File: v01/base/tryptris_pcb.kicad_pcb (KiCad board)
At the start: 2 copper layers, 298.8 x 122 mm, 141 parts, among them J1 USB_C_Receptacle_USB2.0, J2 I2C-L, J3 I2C-R, SW1 Reset, U1 ATmega32U4, U2 MCP23017, U4 HOLE, Y1 16Mhz

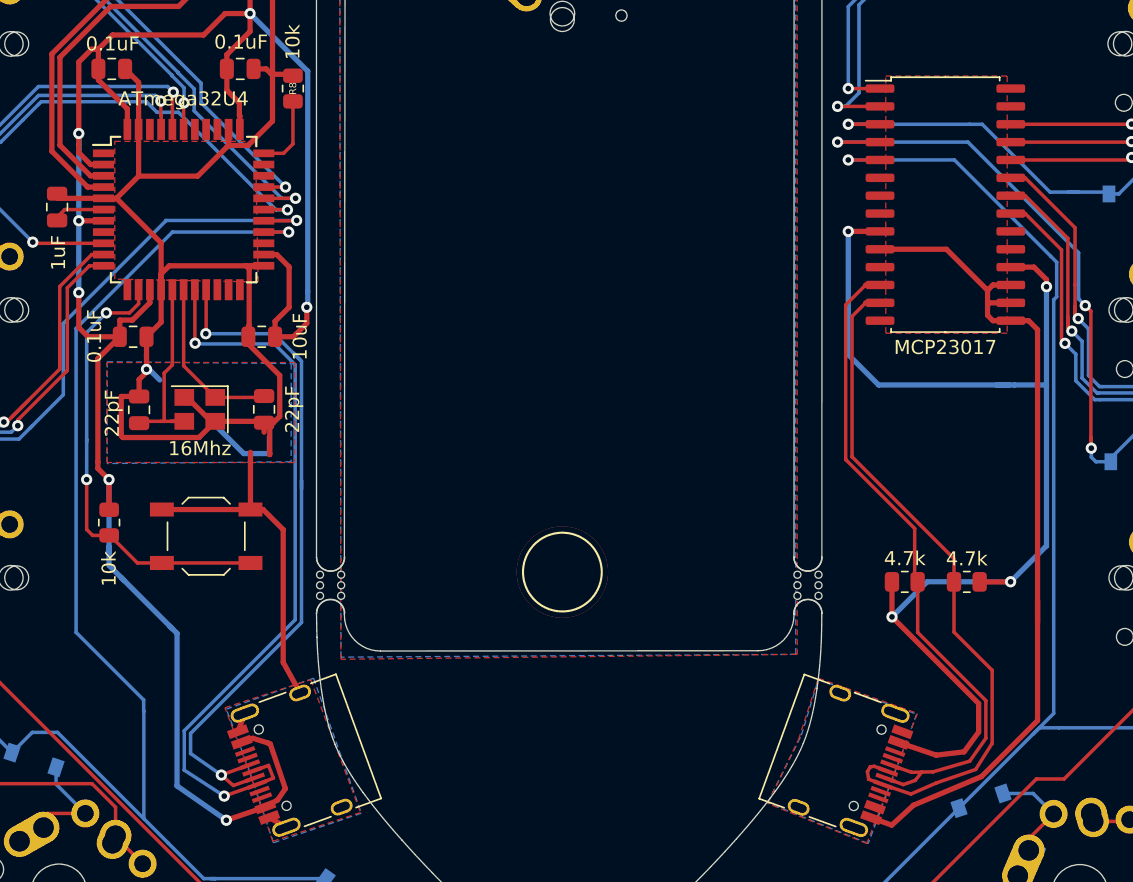
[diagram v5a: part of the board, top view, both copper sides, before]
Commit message: Move I2C resistors to MCU side
This lets the right side be simpler and visually cleaner. It also
matches the component layout of the bling version.
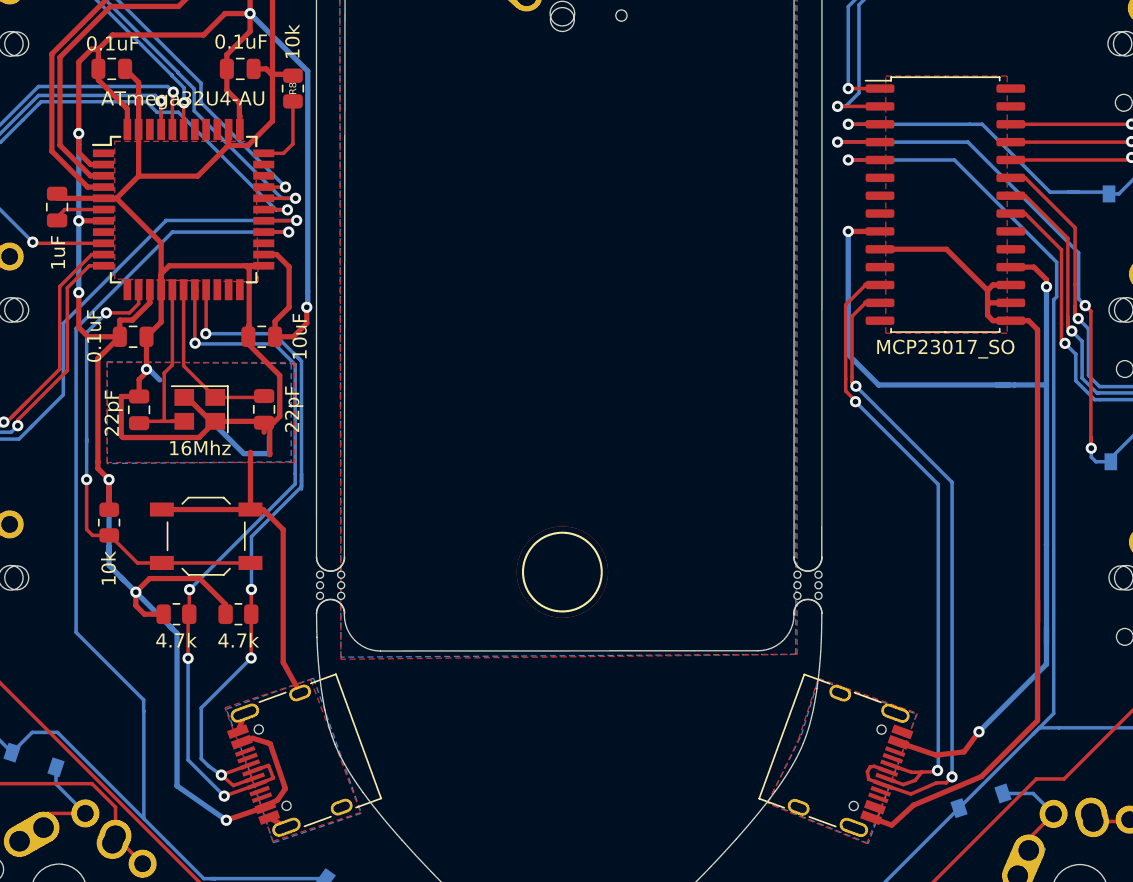
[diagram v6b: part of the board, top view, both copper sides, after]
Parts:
- U1: value ATmega32U4 -> ATmega32U4-AU
- U2: value MCP23017 -> MCP23017_SO
- moved R7 51.9 mm to (152.5, 104.7)
- moved R6 51.9 mm to (148.0, 104.7)
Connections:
- R6 pad 1: SCL-R -> SCL-L
- R6 pad 2: VBUS -> +5V
- R7 pad 1: SDA-R -> +5V
- R7 pad 2: VBUS -> SDA-L
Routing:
- net VBUS: track 84.2 -> 71.8 mm, vias 4 -> 3
- net +5V: track 156.2 -> 167.7 mm, vias 7 -> 8
- net SCL-R: track 48.4 -> 45.4 mm, vias 0 -> 2
- net SDA-R: track 49.7 -> 46.8 mm, vias 0 -> 2
- net SCL-L: track 53.4 -> 53.1 mm, vias 2 -> 4
- net SDA-L: track 50.7 -> 50.4 mm, vias 2 -> 4

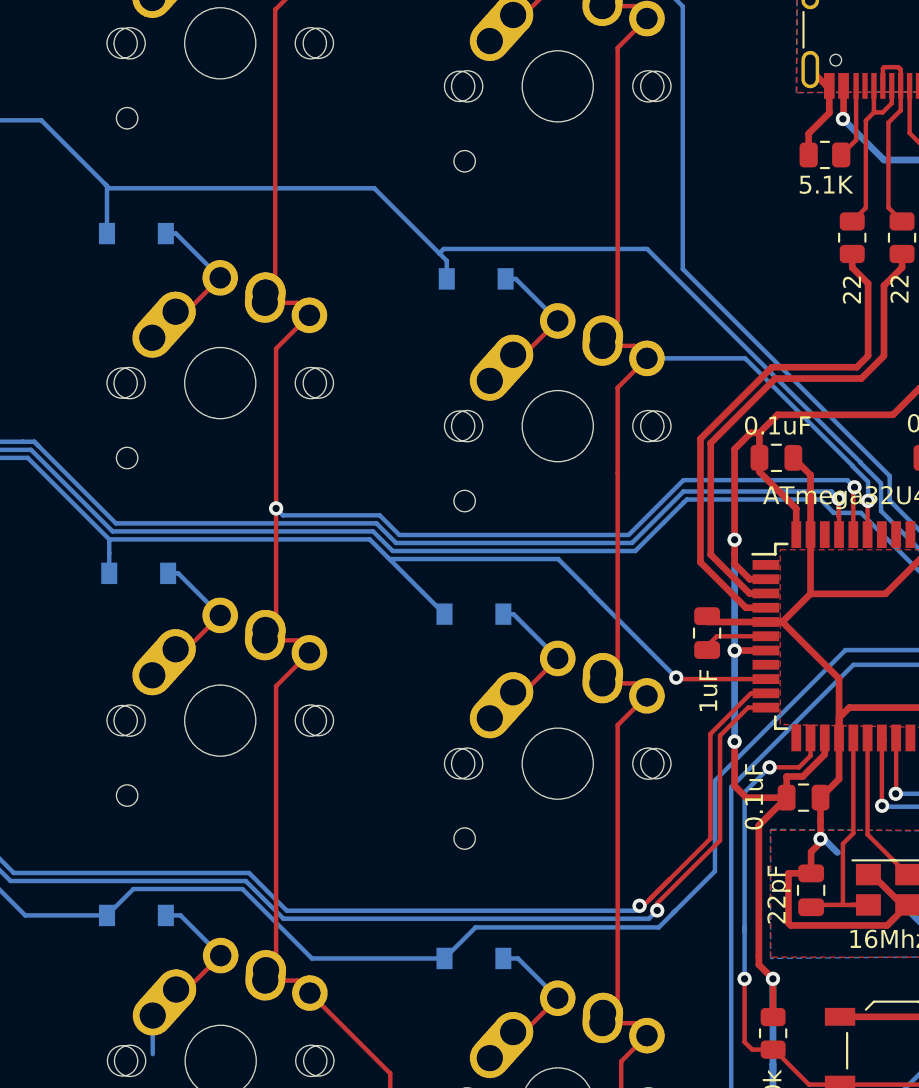
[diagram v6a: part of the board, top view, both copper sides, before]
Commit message: Add ISP connector to base board.
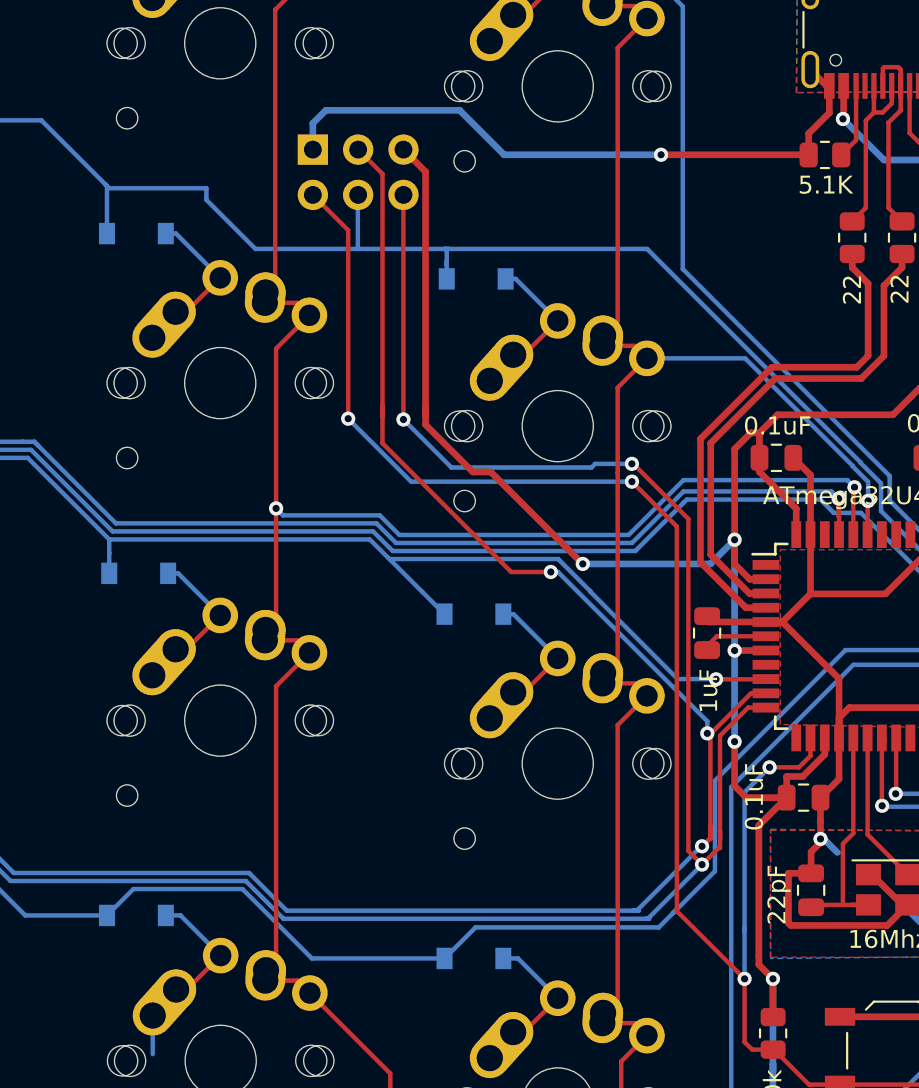
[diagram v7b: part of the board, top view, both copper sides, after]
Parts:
- added J4: AVR-ISP-6, random-keyboard-parts:Reset_Pretty-Mask, B.Cu at (120.0, 49.9)
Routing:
- net Net-(J4-Pad5): track 33.0 -> 94.2 mm, vias 2 -> 4
- net Col0: track 187.4 -> 238.9 mm, vias 2 -> 4
- net Col1: track 171.7 -> 214.3 mm, vias 2 -> 4
- net +5V: track 167.7 -> 205.3 mm, vias 8 -> 9
- net GND: track 158.1 -> 188.7 mm, vias 1 -> 2
- net Row1-L: track 154.0 -> 157.8 mm

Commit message: Fix ISP wiring
I got the pins wrong.
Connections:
- J4 pad 3: Row1-L -> Row2-L
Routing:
- net Row2-L: track 132.2 -> 153.8 mm, vias 1 -> 2
- net Row1-L: track 157.8 -> 154.8 mm
